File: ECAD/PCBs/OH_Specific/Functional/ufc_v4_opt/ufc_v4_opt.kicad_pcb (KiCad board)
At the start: 2 copper layers, 90.1 x 40.2 mm, 137 parts, among them J1 Conn_01x05_Male, J2 Conn_01x05_Male, J3 Conn_01x05_Male, J4 Conn_01x05_Male

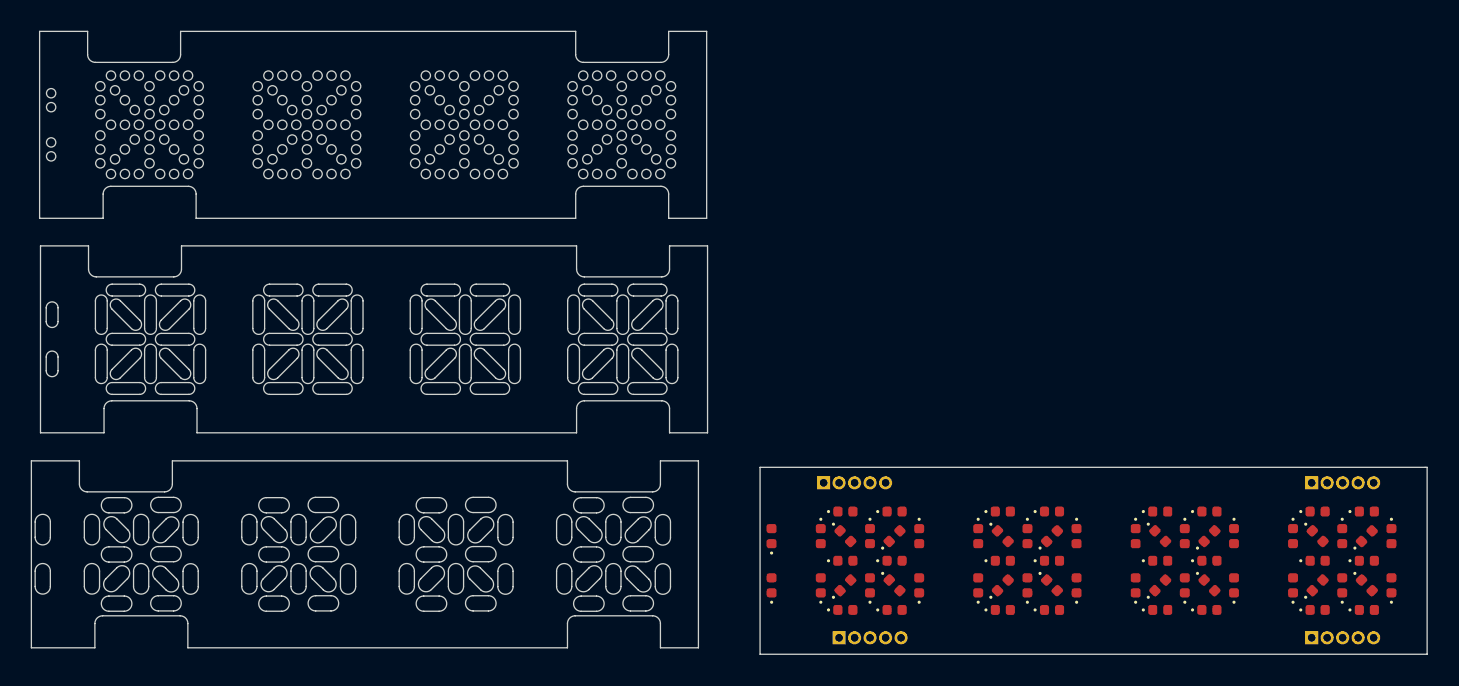
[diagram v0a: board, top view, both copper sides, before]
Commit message: Removed mechanical layers
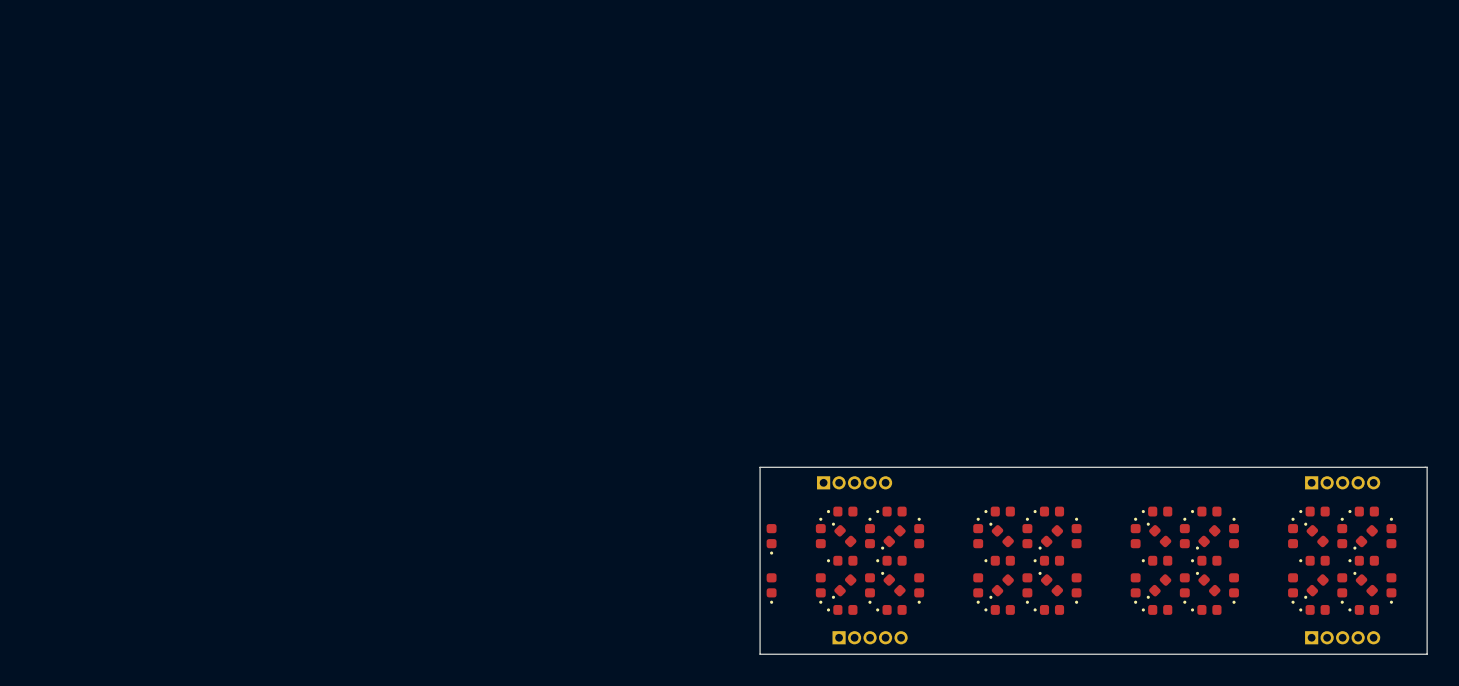
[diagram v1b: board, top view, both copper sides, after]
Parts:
- removed the D1 at (105.1, 58.3)
- removed the D10 at (109.8, 56.8)
- removed the D11 at (109.8, 58.3)
- removed the D12 at (109.8, 59.9)
- removed the D13 at (109.8, 61.5)
- removed the D14 at (109.8, 63.1)
- removed the D15 at (111.4, 58.3)
- removed the D16 at (111.4, 61.5)
- removed the D17 at (115.2, 58.3)
- removed the D18 at (115.2, 61.5)
- removed the D19 at (116.8, 56.8)
- removed the D2 at (105.1, 61.5)
- removed the D20 at (116.8, 58.3)
- removed the D21 at (116.8, 59.9)
- removed the D22 at (116.8, 61.5)
- removed the D23 at (116.8, 63.1)
- removed the D24 at (118.4, 58.3)
- removed the D25 at (118.4, 61.5)
- removed the D26 at (120.0, 56.8)
- removed the D27 at (120.0, 58.3)
- removed the D28 at (120.0, 59.9)
- removed the D29 at (120.0, 61.5)
- removed the D3 at (106.6, 56.8)
- removed the D30 at (120.0, 63.1)
- removed the D31 at (121.6, 58.3)
- removed the D32 at (121.6, 61.5)
- removed the D33 at (125.4, 58.3)
- removed the D34 at (125.4, 61.5)
- removed the D35 at (127.0, 56.8)
- removed the D36 at (127.0, 58.3)
- removed the D37 at (127.0, 59.9)
- removed the D38 at (127.0, 61.5)
- removed the D39 at (127.0, 63.1)
- removed the D4 at (106.6, 58.3)
- removed the D40 at (128.6, 58.3)
- removed the D41 at (128.6, 61.5)
- removed the D42 at (130.1, 56.8)
- removed the D43 at (130.1, 58.3)
- removed the D44 at (130.1, 59.9)
- removed the D45 at (130.1, 61.5)
- removed the D46 at (130.1, 63.1)
- removed the D47 at (131.7, 58.3)
- removed the D48 at (131.7, 61.5)
- removed the D49 at (135.5, 58.3)
- removed the D5 at (106.6, 59.9)
- removed the D50 at (135.5, 61.5)
- removed the D51 at (137.1, 56.8)
- removed the D52 at (137.1, 58.3)
- removed the D53 at (137.1, 59.9)
- removed the D54 at (137.1, 61.5)
- removed the D55 at (137.1, 63.1)
- removed the D56 at (138.7, 58.3)
- removed the D57 at (138.7, 61.5)
- removed the D58 at (140.3, 56.8)
- removed the D59 at (140.3, 58.3)
- removed the D6 at (106.6, 61.5)
- removed the D60 at (140.3, 59.9)
- removed the D61 at (140.3, 61.5)
- removed the D62 at (140.3, 63.1)
- removed the D63 at (141.9, 58.3)
- removed the D64 at (141.9, 61.5)
- removed the D65 at (101.9, 58.3)
- removed the D66 at (101.9, 61.5)
- removed the D7 at (106.6, 63.1)
- removed the D8 at (108.2, 58.3)
- removed the D9 at (108.2, 61.5)
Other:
- board size 90.1 x 40.2 mm -> 43.1 x 12.1 mm
- board text removed: "LAYER 2 / LED SPACER CC BY-NC-SA"
- board text removed: "LAYER 3 / MATRIX LIGHT CHANNELS CC BY-NC-SA"
- board text removed: "LAYER 4 / MATRIX LIGHT CHANNELS CC BY-NC-SA"
- board text removed: "THIS SIDE DOWN"

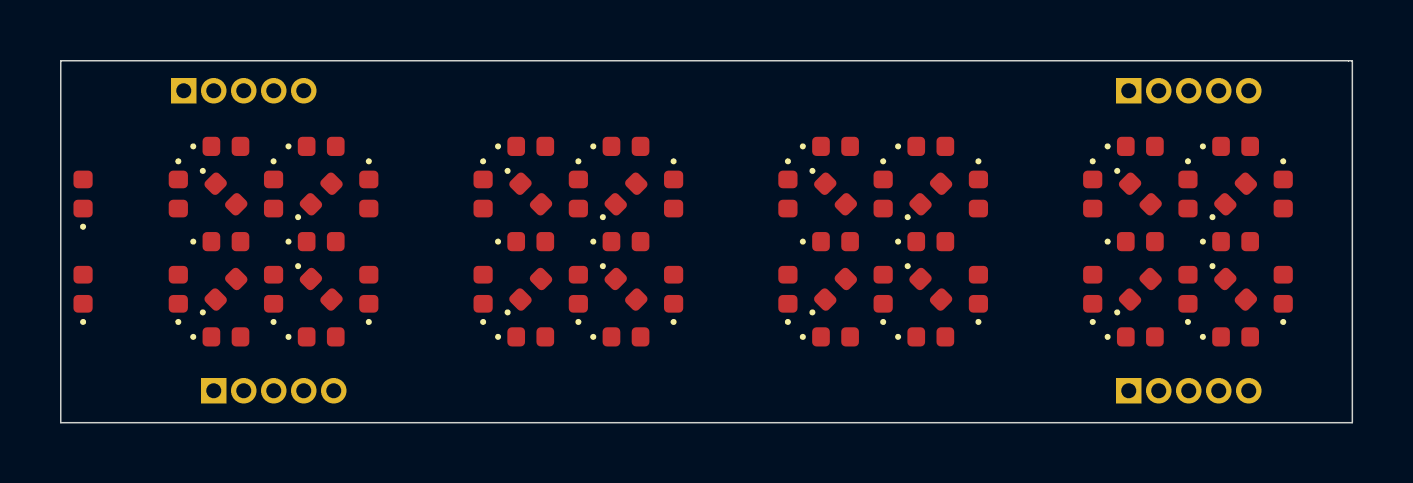
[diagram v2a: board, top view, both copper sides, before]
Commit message: OPT display routed.
Need to add to display panel.
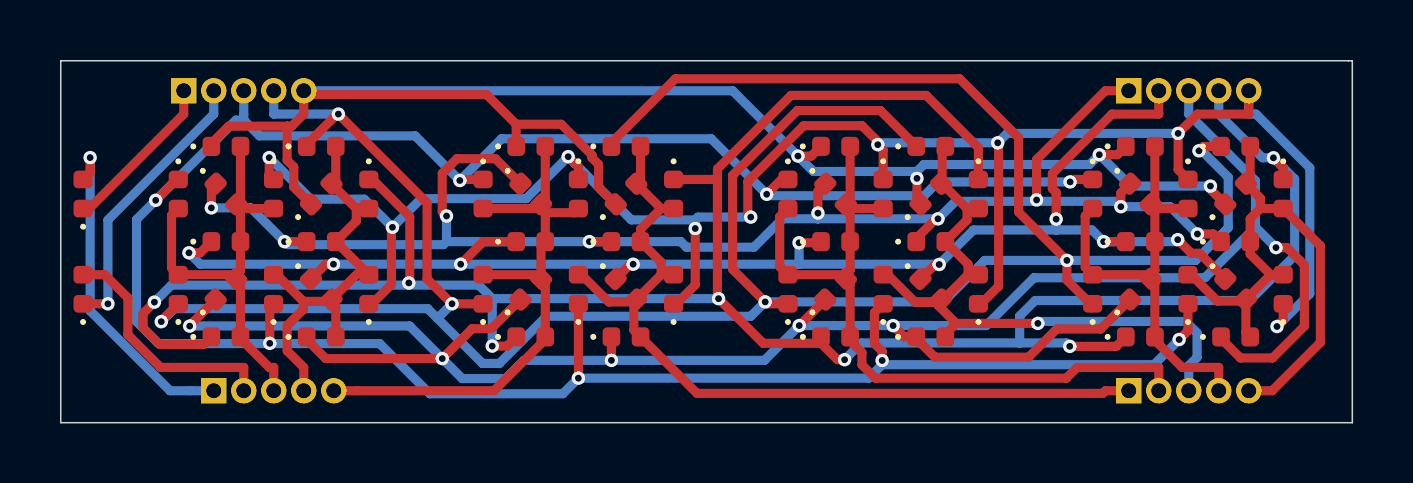
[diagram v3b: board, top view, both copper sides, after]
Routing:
- net /DIG1: track 0.00 -> 92.1 mm, vias 0 -> 6
- net /DIG0: track 0.00 -> 86.7 mm, vias 0 -> 8
- net /DIG6: track 0.00 -> 80.4 mm, vias 0 -> 7
- net /DIG5: track 0.00 -> 72.3 mm, vias 0 -> 6
- net /DIG7: track 0.00 -> 65.7 mm, vias 0 -> 9
- net /DIG2: track 0.00 -> 56.3 mm, vias 0 -> 4
- net /DIG3: track 0.00 -> 52.0 mm, vias 0 -> 9
- net /DIG4: track 0.00 -> 50.8 mm, vias 0 -> 9
- net /SEGC: track 0.00 -> 27.9 mm
- net /SEGD: track 0.00 -> 24.2 mm
- net /SEGE: track 0.00 -> 21.4 mm, vias 0 -> 1
- net /SEGB: track 0.00 -> 19.5 mm
- net /SEGG: track 0.00 -> 18.9 mm
- net /SEGF: track 0.00 -> 15.4 mm
- net /SEGDP: track 0.00 -> 14.4 mm
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
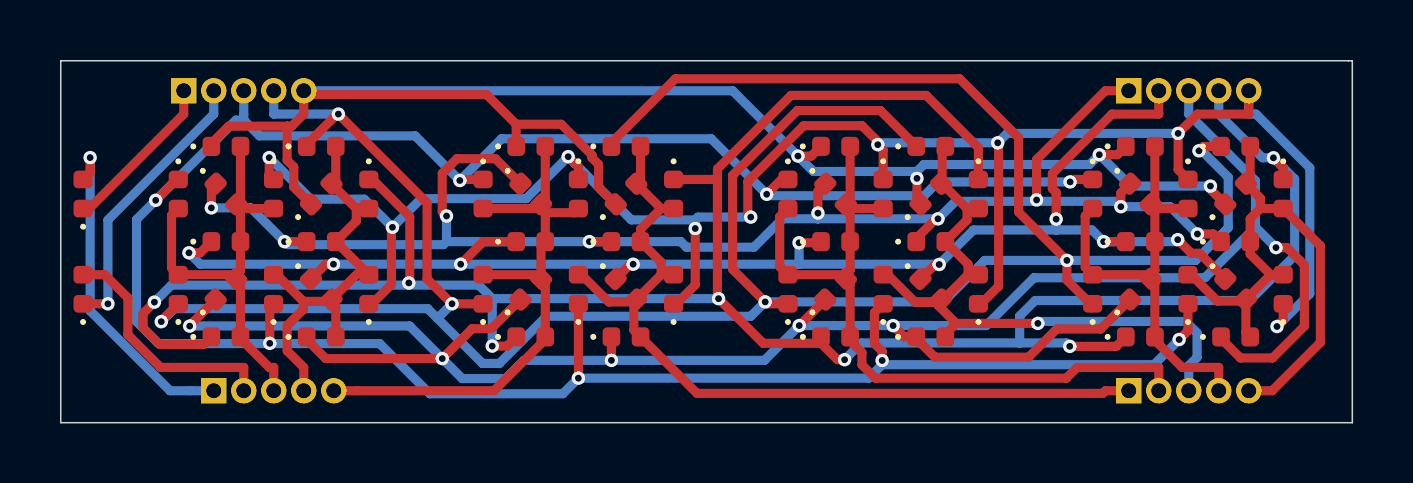
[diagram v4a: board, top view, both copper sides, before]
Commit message: New UFC Disp Panel
Added missing OPT display to panel. Optimized panel, generated new manufacturing files. Next will generate light channel PCB layers for all displays and generate MCAD for displays and start updating UFC MCAD to define main UFC PCB requirements.
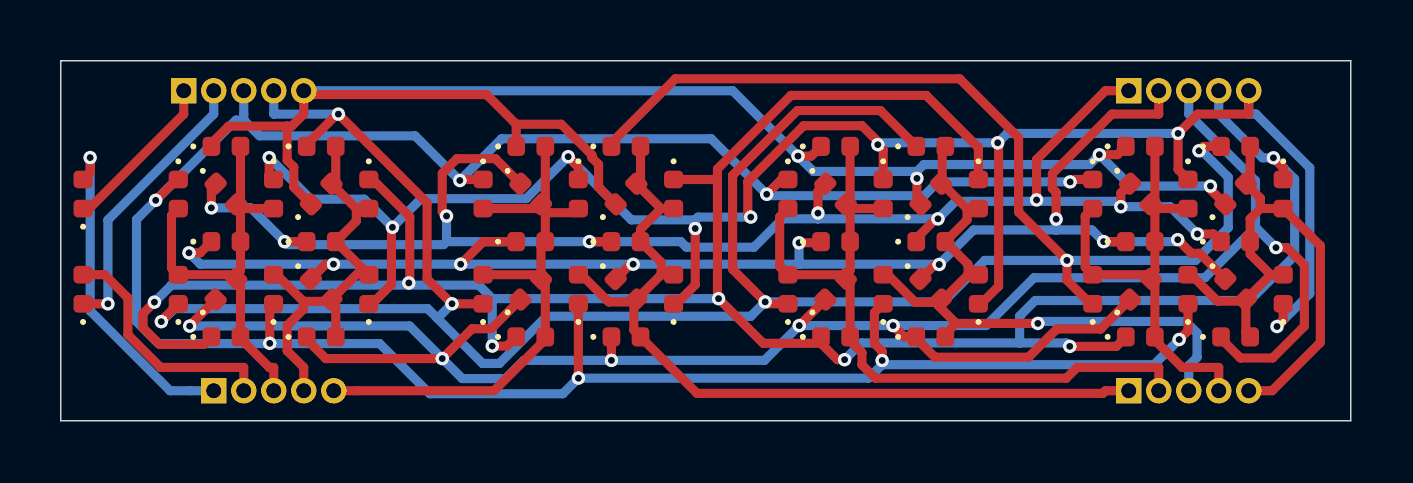
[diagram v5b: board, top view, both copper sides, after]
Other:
- board size 43.1 x 12.1 mm -> 43 x 12 mm
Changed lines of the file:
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@@
   (general
     (thickness 1.6)
-    (drawings 28)
+    (drawings 27)
     (tracks 601)
     (zones 0)
@@
     )
   )
+  (gr_line (start 190.6375 94.042) (end 190.6375 82.042) (layer Edge.Cuts) (width 0.05))
   (gr_text "REV: 1" (at 189.7375 88.042 90) (layer B.SilkS)
     (effects (font (size 0.6 0.6) (thickness 0.15)) (justify mirror))
@@
     (effects (font (size 0.6 0.6) (thickness 0.12)) (justify left mirror))
   )
-  (gr_line (start 190.6905 82.042) (end 190.5635 82.042) (layer Edge.Cuts) (width 0.05))
-  (gr_line (start 190.6905 94.107) (end 190.6905 82.042) (layer Edge.Cuts) (width 0.05))
-  (gr_line (start 147.6375 94.107) (end 190.6905 94.107) (layer Edge.Cuts) (width 0.05))
-  (gr_line (start 147.6375 82.042) (end 147.6375 94.107) (layer Edge.Cuts) (width 0.05))
-  (gr_line (start 190.5635 82.042) (end 147.6375 82.042) (layer Edge.Cuts) (width 0.05))
+  (gr_line (start 147.6375 94.042) (end 190.6375 94.042) (layer Edge.Cuts) (width 0.05))
+  (gr_line (start 147.6375 82.042) (end 147.6375 94.042) (layer Edge.Cuts) (width 0.05))
+  (gr_line (start 190.6375 82.042) (end 147.6375 82.042) (layer Edge.Cuts) (width 0.05))
   (segment (start 174.8731 84.8397) (end 174.8731 84.7357) (width 0.305) (layer F.Cu) (net 1))
   (segment (start 174.8731 84.7357) (end 174.3451 84.2077) (width 0.305) (layer F.Cu) (net 1))

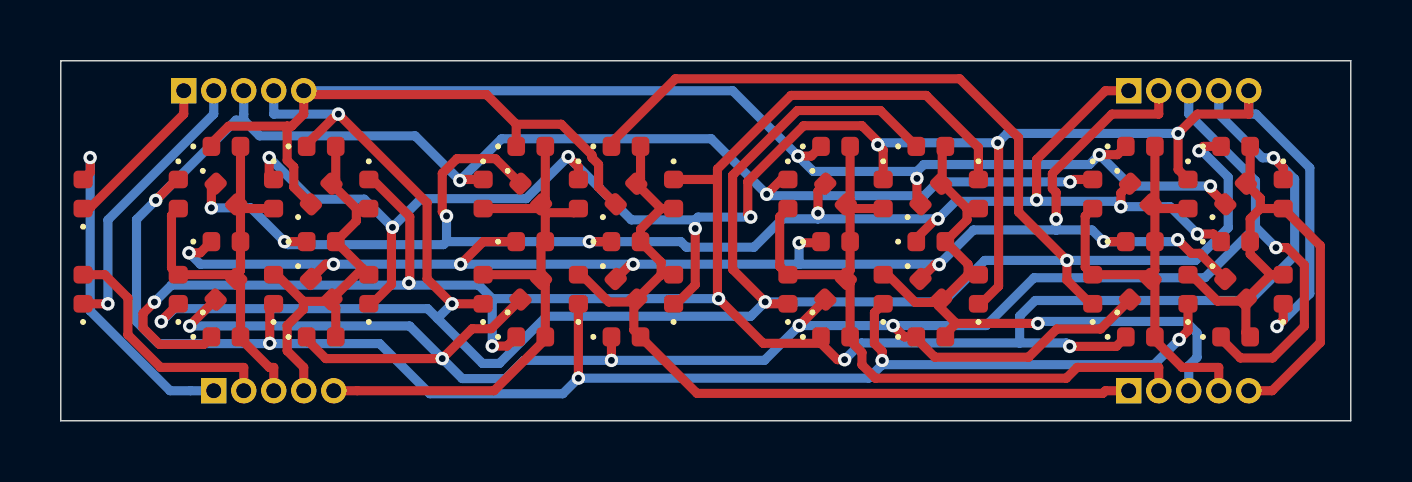
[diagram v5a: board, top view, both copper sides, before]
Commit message: modified opt boards to better track digits. now each dot matrix digit is composed by two digits. added a spreadsheet to calculate the characters.
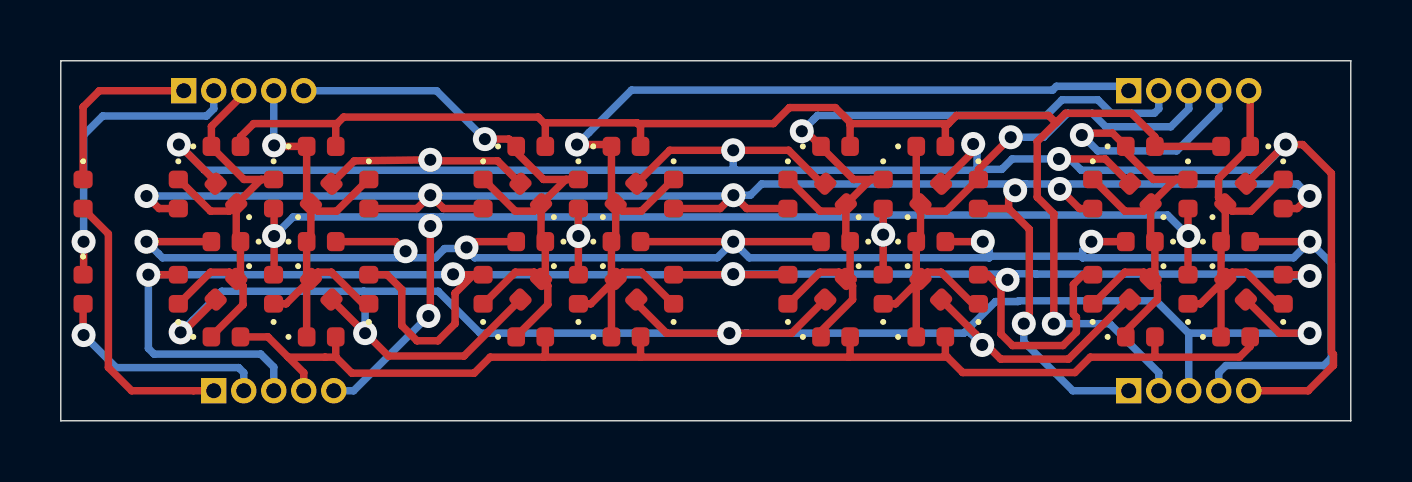
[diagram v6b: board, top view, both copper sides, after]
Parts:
- turned D20 to 135 degrees
- turned D21 to 180 degrees
- turned D22 to 225 degrees
- turned D36 to 135 degrees
- turned D37 to 180 degrees
- turned D38 to 225 degrees
- turned D4 to 135 degrees
- turned D5 to 180 degrees
- turned D52 to 135 degrees
- turned D53 to 180 degrees
- turned D54 to 225 degrees
- turned D58 to 180 degrees
- turned D6 to 225 degrees
- turned D65 to 270 degrees
- turned D66 to 270 degrees
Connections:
- D1 pad 2: /SEGDP -> /SEGC
- D10 pad 2: /SEGA -> /SEGD
- D11 pad 1: /DIG2 -> /DIG1
- D11 pad 2: /SEGA -> /SEGG
- D12 pad 1: /DIG3 -> /DIG1
- D12 pad 2: /SEGA -> /SEGF
- D13 pad 1: /DIG4 -> /DIG1
- D13 pad 2: /SEGA -> /SEGE
- D14 pad 1: /DIG5 -> /DIG1
- D15 pad 1: /DIG6 -> /DIG1
- D15 pad 2: /SEGA -> /SEGC
- D16 pad 1: /DIG7 -> /DIG1
- D16 pad 2: /SEGA -> /SEGDP
- D17 pad 1: /DIG0 -> /DIG2
- D17 pad 2: /SEGB -> /SEGC
- D18 pad 1: /DIG1 -> /DIG2
- D18 pad 2: /SEGB -> /SEGDP
- D19 pad 2: /SEGB -> /SEGD
- D2 pad 1: /DIG1 -> /DIG0
- D20 pad 1: /DIG3 -> /DIG2
- D20 pad 2: /SEGB -> /SEGG
- D21 pad 1: /DIG4 -> /DIG2
- D21 pad 2: /SEGB -> /SEGF
- D22 pad 1: /DIG5 -> /DIG2
- D22 pad 2: /SEGB -> /SEGE
- D23 pad 1: /DIG6 -> /DIG2
- D23 pad 2: /SEGB -> /SEGA
- D24 pad 1: /DIG7 -> /DIG2
- D25 pad 1: /DIG0 -> /DIG3
- D25 pad 2: /SEGC -> /SEGB
- D26 pad 1: /DIG1 -> /DIG3
- D26 pad 2: /SEGC -> /SEGD
- D27 pad 1: /DIG2 -> /DIG3
- D27 pad 2: /SEGC -> /SEGG
- D28 pad 2: /SEGC -> /SEGF
- D29 pad 1: /DIG4 -> /DIG3
- D29 pad 2: /SEGC -> /SEGE
- D3 pad 1: /DIG2 -> /DIG0
- D3 pad 2: /SEGDP -> /SEGD
- D30 pad 1: /DIG5 -> /DIG3
- D30 pad 2: /SEGC -> /SEGA
- D31 pad 1: /DIG6 -> /DIG3
- D32 pad 1: /DIG7 -> /DIG3
- D32 pad 2: /SEGC -> /SEGDP
- D33 pad 1: /DIG0 -> /DIG4
- D33 pad 2: /SEGD -> /SEGC
- D34 pad 1: /DIG1 -> /DIG4
- D34 pad 2: /SEGD -> /SEGDP
- D35 pad 1: /DIG2 -> /DIG4
- D36 pad 1: /DIG3 -> /DIG4
- D36 pad 2: /SEGD -> /SEGG
- D37 pad 2: /SEGD -> /SEGF
- D38 pad 1: /DIG5 -> /DIG4
- D38 pad 2: /SEGD -> /SEGE
- D39 pad 1: /DIG6 -> /DIG4
- D39 pad 2: /SEGD -> /SEGA
- D4 pad 1: /DIG3 -> /DIG0
- D4 pad 2: /SEGDP -> /SEGG
- D40 pad 1: /DIG7 -> /DIG4
- D40 pad 2: /SEGD -> /SEGB
- D41 pad 1: /DIG0 -> /DIG5
- D41 pad 2: /SEGE -> /SEGB
- D42 pad 1: /DIG1 -> /DIG5
- D42 pad 2: /SEGE -> /SEGD
- D43 pad 1: /DIG2 -> /DIG5
- D43 pad 2: /SEGE -> /SEGG
- D44 pad 1: /DIG3 -> /DIG5
- D44 pad 2: /SEGE -> /SEGF
- D45 pad 1: /DIG4 -> /DIG5
- D46 pad 2: /SEGE -> /SEGA
- D47 pad 1: /DIG6 -> /DIG5
- D47 pad 2: /SEGE -> /SEGC
- D48 pad 1: /DIG7 -> /DIG5
- D48 pad 2: /SEGE -> /SEGDP
- D49 pad 1: /DIG0 -> /DIG6
- D49 pad 2: /SEGF -> /SEGC
- D5 pad 1: /DIG4 -> /DIG0
- D5 pad 2: /SEGDP -> /SEGF
- D50 pad 1: /DIG1 -> /DIG6
- D50 pad 2: /SEGF -> /SEGDP
- D51 pad 1: /DIG2 -> /DIG6
- D51 pad 2: /SEGF -> /SEGD
- D52 pad 1: /DIG3 -> /DIG6
- D52 pad 2: /SEGF -> /SEGG
- D53 pad 1: /DIG4 -> /DIG6
- D54 pad 1: /DIG5 -> /DIG6
- D54 pad 2: /SEGF -> /SEGE
- D55 pad 2: /SEGF -> /SEGA
- D56 pad 1: /DIG7 -> /DIG6
- D56 pad 2: /SEGF -> /SEGB
- D57 pad 1: /DIG0 -> /DIG7
- D57 pad 2: /SEGG -> /SEGB
- D58 pad 1: /DIG1 -> /DIG7
- D58 pad 2: /SEGG -> /SEGD
- D59 pad 1: /DIG2 -> /DIG7
- D6 pad 1: /DIG5 -> /DIG0
- D6 pad 2: /SEGDP -> /SEGE
- D60 pad 1: /DIG3 -> /DIG7
- D60 pad 2: /SEGG -> /SEGF
- D61 pad 1: /DIG4 -> /DIG7
- D61 pad 2: /SEGG -> /SEGE
- D62 pad 1: /DIG5 -> /DIG7
- D62 pad 2: /SEGG -> /SEGA
- D63 pad 1: /DIG6 -> /DIG7
- D63 pad 2: /SEGG -> /SEGC
- D64 pad 2: /SEGG -> /SEGDP
- D7 pad 1: /DIG6 -> /DIG0
- D7 pad 2: /SEGDP -> /SEGA
- D8 pad 1: /DIG7 -> /DIG0
- D8 pad 2: /SEGDP -> /SEGB
- D9 pad 1: /DIG0 -> /DIG1
- D9 pad 2: /SEGA -> /SEGB
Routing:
- net /DIG1: track 92.1 -> 16.5 mm, vias 6 -> 1
- net /DIG0: track 86.7 -> 16.6 mm, vias 8 -> 0
- net /DIG6: track 80.4 -> 21.9 mm, vias 7 -> 1
- net /SEGG: track 18.9 -> 74.3 mm, vias 0 -> 6
- net /SEGDP: track 14.4 -> 68.2 mm, vias 0 -> 5
- net /SEGF: track 15.4 -> 67.1 mm, vias 0 -> 7
- net /SEGE: track 21.4 -> 71.8 mm, vias 1 -> 5
- net /DIG7: track 65.7 -> 15.6 mm, vias 9 -> 0
- net /DIG5: track 72.3 -> 22.2 mm, vias 6 -> 1
- net /SEGC: track 27.9 -> 62.5 mm, vias 0 -> 7
- net /DIG2: track 56.3 -> 22.1 mm, vias 4 -> 1
- net /SEGB: track 19.5 -> 48.9 mm, vias 0 -> 6
- net /SEGD: track 24.2 -> 50.7 mm, vias 0 -> 1
- net /SEGA: track 14.3 -> 40.8 mm
- net /DIG4: track 50.8 -> 28.1 mm, vias 9 -> 1
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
